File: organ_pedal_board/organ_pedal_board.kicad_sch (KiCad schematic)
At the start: 19 parts, among them J1 AudioPlug3, J2 AudioPlug3, U1 MCP6002-xSN, U3 ADS1115IDGS, U4 AP2112K-3.3

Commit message: Feat: added OLED circuit to board schematics
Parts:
- added J3: Conn_01x04, symbol Connector_Generic:Conn_01x04
- added R5, R6: 4k7, symbol Device:R
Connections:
- net GND: now also J3.1 (Pin_1)
- net dready: no longer U2.15 (D23)
- net i2c_scl: now also J3.3 (Pin_3), R6.1
- net i2c_sda: now also J3.4 (Pin_4), R5.2
- new net +3V3: J3.2 (Pin_2), R5.1, R6.2
- no-connect marks 24 -> 25
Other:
- note added: "ESP32 DevKit V1"
- note added: "OLED"
- note added: "OLED pins"
- moved on the sheet: J1, J2

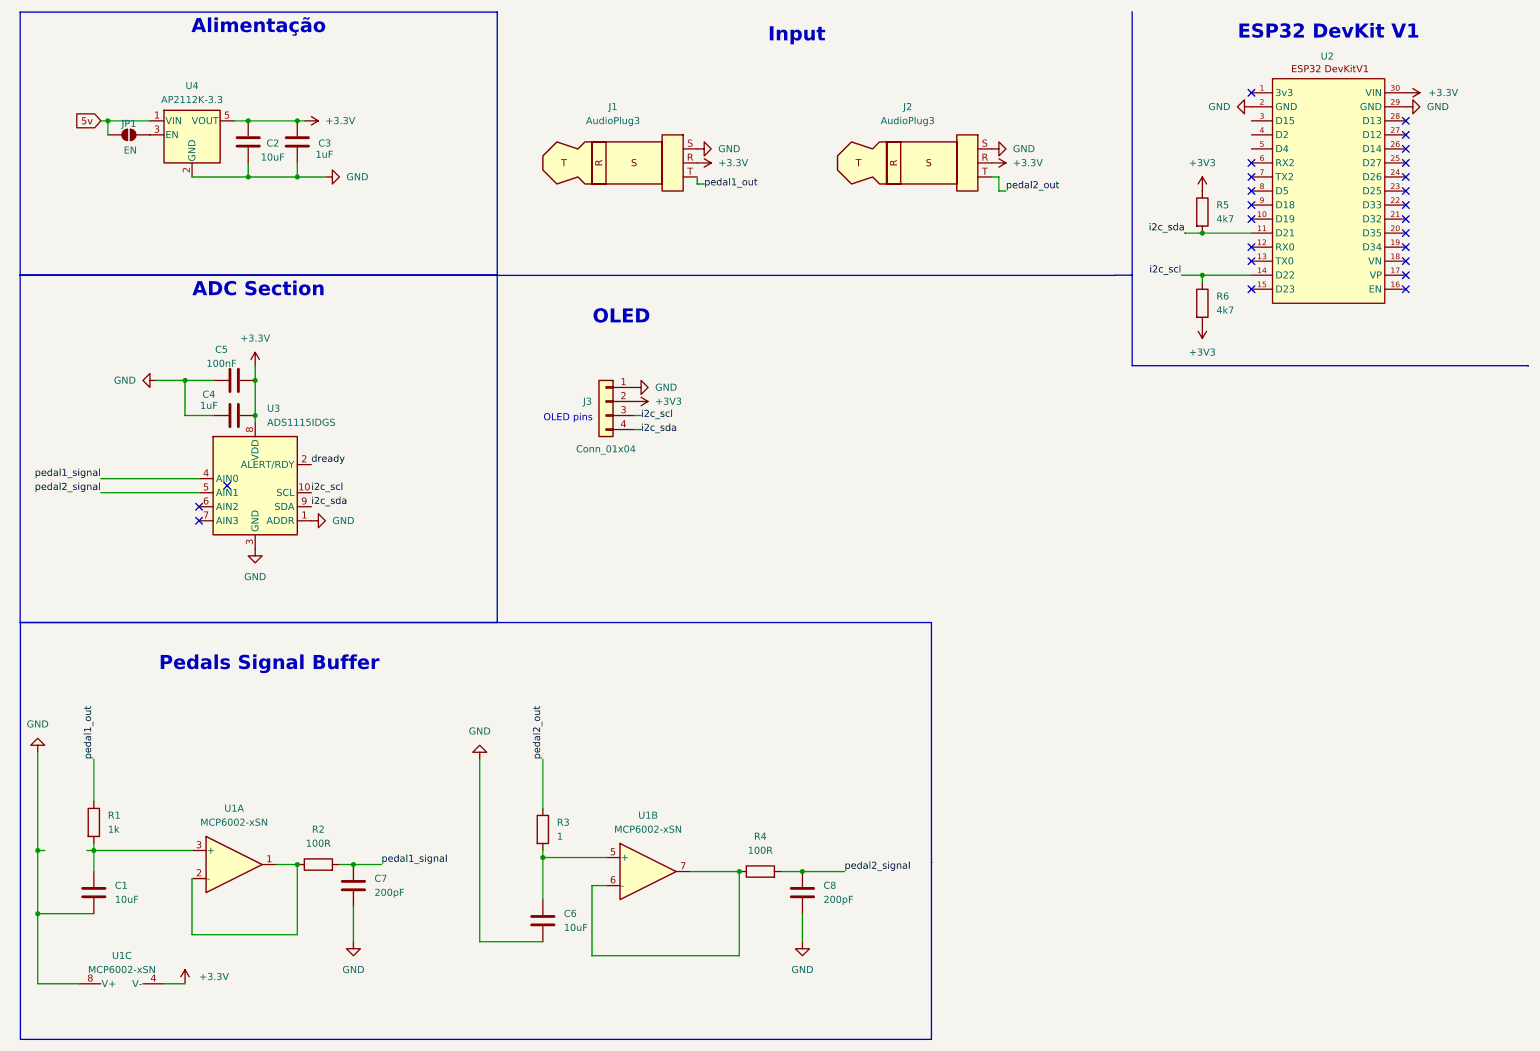
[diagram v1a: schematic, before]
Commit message: Feat: added 8 buttons and finished schematics.
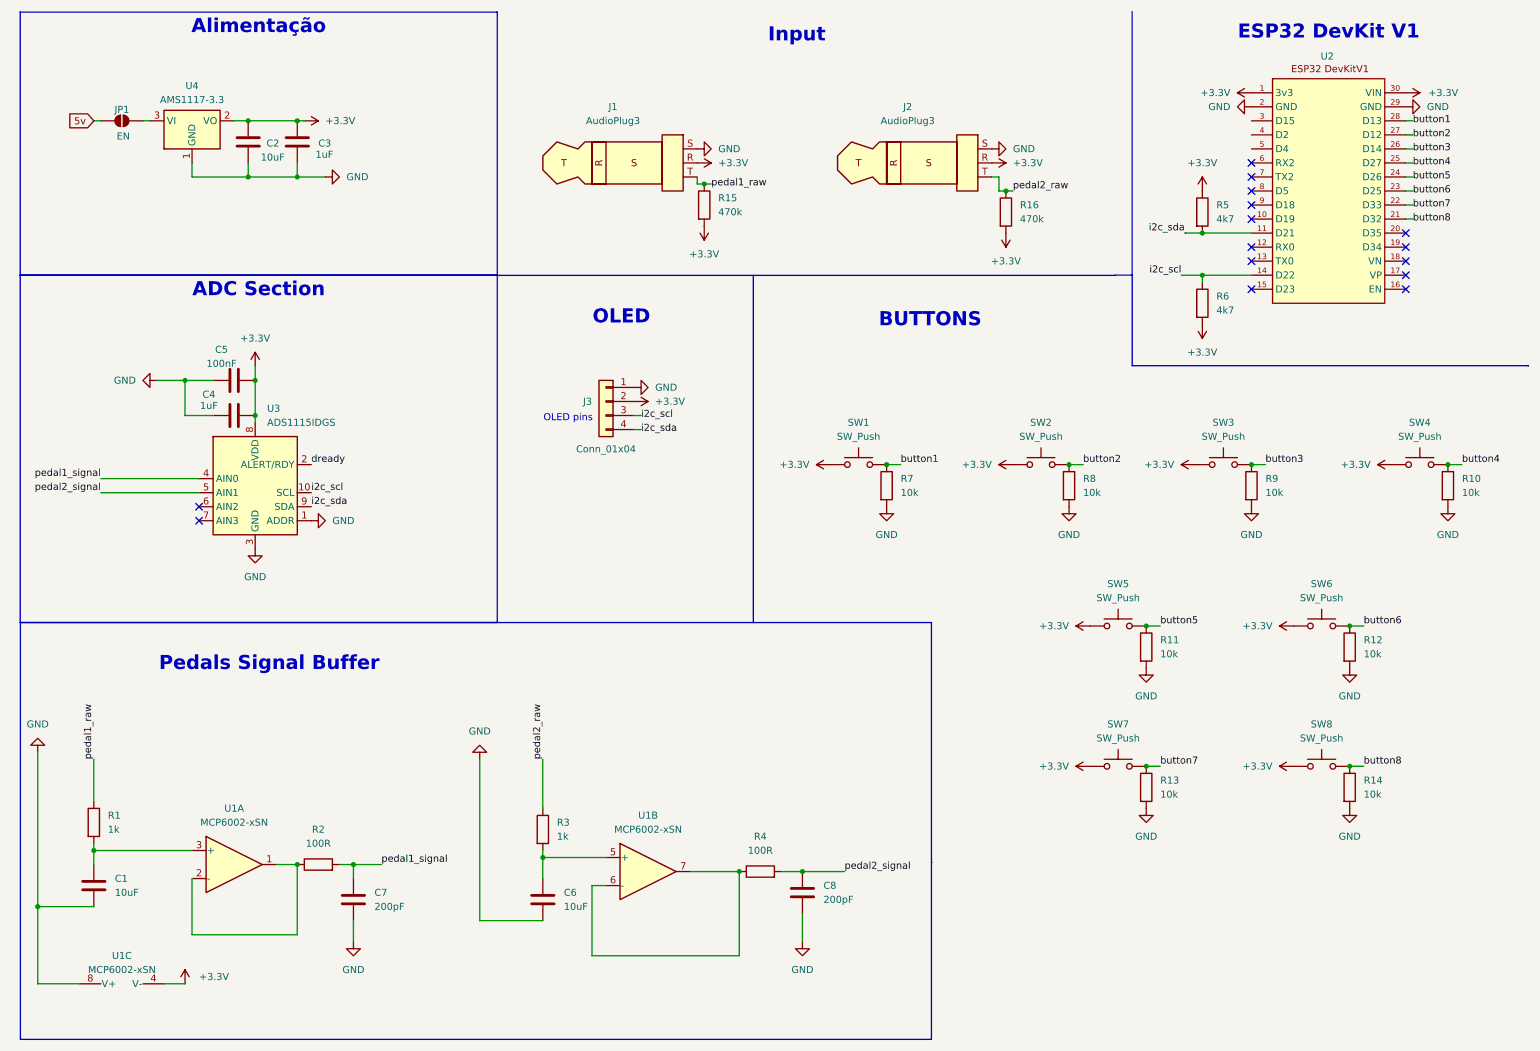
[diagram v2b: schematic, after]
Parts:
- removed U4: AP2112K-3.3, Package_TO_SOT_SMD:SOT-23-5, symbol Regulator_Linear:AP2112K-3.3
- added R10, R11, R12, R13, R14, R7, R8, R9: 10k, Resistor_THT:R_Axial_DIN0207_L6.3mm_D2.5mm_P7.62mm_Horizontal, symbol Device:R
- added R15, R16: 470k, Resistor_THT:R_Axial_DIN0207_L6.3mm_D2.5mm_P7.62mm_Horizontal, symbol Device:R
- added SW1, SW2, SW3, SW4, SW5, SW6, SW7, SW8: SW_Push, symbol Switch:SW_Push
- added U4: AMS1117-3.3, Package_TO_SOT_SMD:SOT-223-3_TabPin2, symbol Regulator_Linear:AMS1117-3.3
- C1, C2, C3, C4, C5, C6, C7, C8: footprint (none) -> Capacitor_THT:C_Disc_D10.5mm_W5.0mm_P10.00mm
- R1, R2, R4, R5, R6: footprint (none) -> Resistor_THT:R_Axial_DIN0207_L6.3mm_D2.5mm_P7.62mm_Horizontal
- R3: value 1 -> 1k; footprint (none) -> Resistor_THT:R_Axial_DIN0207_L6.3mm_D2.5mm_P7.62mm_Horizontal
- U1: footprint (none) -> Package_SO:SOIC-8_3.9x4.9mm_P1.27mm
- U3: footprint Package_SO:TSSOP-10_3x3mm_P0.5mm -> (none)
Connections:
- net +3V3 is gone; now on net +3.3V: J3.2 (Pin_2), R5.1, R6.2
- net +3.3V: now also U2.1 (3v3), R15.2, R16.2, SW1.1, SW2.1, SW3.1, SW4.1, SW5.1, SW6.1, SW7.1, SW8.1, U4.2 (VO)
- net GND: now also R10.2, R11.2, R12.2, R13.2, R14.2, R7.2, R8.2, R9.2, U4.1 (GND)
- net at JP1.2 (B): now also U4.3 (VI)
- net button8: now reaches U2.21 (D32)
- net button8: now also R14.1, SW8.2
- net button7: now reaches U2.22 (D33)
- net button7: now also R13.1, SW7.2
- net button6: now reaches U2.23 (D25)
- net button6: now also R12.1, SW6.2
- net button5: now reaches U2.24 (D26)
- net button5: now also R11.1, SW5.2
- net button4: now reaches U2.25 (D27)
- net button4: now also R10.1, SW4.2
- net button3: now reaches U2.26 (D14)
- net button3: now also R9.1, SW3.2
- net button2: now reaches U2.27 (D12)
- net button2: now also R8.1, SW2.2
- net button1: now reaches U2.28 (D13)
- net button1: now also R7.1, SW1.2
- net pedal1_out renamed pedal1_raw
- net pedal1_raw: now also R15.1
- net pedal2_out renamed pedal2_raw
- net pedal2_raw: now also R16.1
- no-connect marks 25 -> 15
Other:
- note added: "BUTTONS"
- title: (none) -> ESP32_MIDI_Controller
- moved on the sheet: C1, C6, C7, JP1

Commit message: Refactor code structure for improved readability and maintainability
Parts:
- removed C2: 10uF, Capacitor_THT:C_Disc_D10.5mm_W5.0mm_P10.00mm, symbol Device:C
- removed C3: 1uF, Capacitor_THT:C_Disc_D10.5mm_W5.0mm_P10.00mm, symbol Device:C
- removed J1, J2: AudioPlug3, symbol Connector_Audio:AudioPlug3
- removed JP1: EN, symbol Jumper:SolderJumper_2_Open
- removed U3: ADS1115IDGS, symbol Analog_ADC:ADS1115IDGS
- removed U4: AMS1117-3.3, Package_TO_SOT_SMD:SOT-223-3_TabPin2, symbol Regulator_Linear:AMS1117-3.3
- added J2, J3: NMJ6HFD2, Connector_Audio:Jack_6.35mm_Neutrik_NMJ6HFD2_Horizontal, symbol Connector_Audio:NMJ6HFD2
- added J4: ADS1115_conn, Connector_PinSocket_2.54mm:PinSocket_1x10_P2.54mm_Vertical, symbol Connector_Generic:Conn_01x10
- added R17: 10k, Resistor_THT:R_Axial_DIN0207_L6.3mm_D2.5mm_P5.08mm_Vertical, symbol Device:R
- added SW9: SW_Push, Button_Switch_THT:SW_PUSH_6mm, symbol Switch:SW_Push
- J1: renamed from J3; footprint (none) -> Connector_PinSocket_2.54mm:PinSocket_1x04_P2.54mm_Vertical
- R1, R10, R11, R12, R13, R14, R2, R3, R4, R5, R6, R7, R8, R9: footprint Resistor_THT:R_Axial_DIN0207_L6.3mm_D2.5mm_P7.62mm_Horizontal -> Resistor_THT:R_Axial_DIN0207_L6.3mm_D2.5mm_P5.08mm_Vertical
- R15, R16: value 470k -> 10k; footprint Resistor_THT:R_Axial_DIN0207_L6.3mm_D2.5mm_P7.62mm_Horizontal -> Resistor_THT:R_Axial_DIN0207_L6.3mm_D2.5mm_P5.08mm_Vertical
- SW1, SW2, SW3, SW4, SW5, SW6, SW7, SW8: footprint (none) -> Connector_JST:JST_XH_S2B-XH-A-1_1x02_P2.50mm_Horizontal
- U2: footprint (none) -> MyDesigns:esp32_devkit_v1_doit
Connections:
- net +3.3V: now also J2.R, J3.R, J4.1 (Pin_1), SW9.1; no longer U2.30 (VIN)
- net GND: now also J2.S, J3.S, J4.2 (Pin_2), J4.5 (Pin_5), R17.2
- net dready: now also J4.6 (Pin_6)
- net i2c_scl: now also J4.3 (Pin_3)
- net i2c_sda: now also J4.4 (Pin_4)
- net pedal1_raw: now also J2.T; no longer R15.1
- net pedal1_signal: now also J4.7 (Pin_7)
- net pedal2_raw: now also J3.T; no longer R16.1
- net pedal2_signal: now also J4.8 (Pin_8)
- net config_button: now reaches U2.3 (D15)
- net config_button: now also R17.1, SW9.2
- new net: J3.TN, R16.1
- new net: J2.TN, R15.1
- no-connect marks 15 -> 22
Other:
- moved on the sheet: C4, C5, J1, R15, R16, R5, R6

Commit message: Fix: Corrected MCP6002 power supply, corrected P10 plug 1 MCP6002  signal output
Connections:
- net +3.3V: now also C1.2, U1.8 (V+); no longer U1.4 (V-)
- net GND: now also U1.4 (V-); no longer C1.2, U1.8 (V+)
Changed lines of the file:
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@@
 	)
 	(junction
-		(at 19.05 173.99)
-		(diameter 0)
-		(color 0 0 0 0)
-	)
-	(junction
 		(at 252.73 148.59)
 		(diameter 0)
@@
 	)
 	(junction
+		(at 19.05 173.99)
+		(diameter 0)
+		(color 0 0 0 0)
+	)
+	(junction
 		(at 57.15 76.2)
 		(diameter 0)
@@
 	(wire
 		(pts
-			(xy 19.05 146.05) (xy 19.05 173.99)
-		)
-		(stroke
-			(width 0)
-			(type default)
-		)
-	)
-	(wire
-		(pts
 			(xy 57.15 76.2) (xy 60.96 76.2)
 		)
@@
 	(wire
 		(pts
+			(xy 19.05 142.24) (xy 19.05 173.99)
+		)
+		(stroke
+			(width 0)
+			(type default)
+		)
+	)
+	(wire
+		(pts
 			(xy 264.16 36.83) (xy 262.89 36.83)
 		)
@@
 		)
 	)
-	(wire
-		(pts
-			(xy 38.1 187.96) (xy 41.91 187.96)
-		)
-		(stroke
-			(width 0)
-			(type default)
-		)
-	)
 	(polyline
 		(pts
@@
 	(wire
 		(pts
+			(xy 40.64 187.96) (xy 38.1 187.96)
+		)
+		(stroke
+			(width 0)
+			(type default)
+		)
+	)
+	(wire
+		(pts
 			(xy 53.34 83.82) (xy 60.96 83.82)
 		)
@@
 	(symbol
 		(lib_id "power:+5V")
-		(at 41.91 187.96 0)
+		(at 19.05 142.24 0)
 		(unit 1)
 		(exclude_from_sim no)
@@
 		(on_board yes)
 		(dnp no)
-		(fields_autoplaced yes)
 		(property "Reference" "#PWR03"
-			(at 41.91 191.77 0)
+			(at 19.05 146.05 0)
 			(effects
 				(font
@@
 		)
 		(property "Value" "+3.3V"
-			(at 44.45 186.6899 0)
+			(at 19.05 138.176 0)
 			(effects
 				(font
 					(size 1.27 1.27)
 				)
-				(justify left)
+				(justify bottom)
 			)
 		)
 		(property "Footprint" ""
-			(at 41.91 187.96 0)
+			(at 19.05 142.24 0)
 			(effects
 				(font
@@
 		)
 		(property "Datasheet" ""
-			(at 41.91 187.96 0)
+			(at 19.05 142.24 0)
 			(effects
 				(font
@@
 		)
 		(property "Description" ""
-			(at 41.91 187.96 0)
+			(at 19.05 142.24 0)
 			(effects
 				(font
@@
 	(symbol
 		(lib_id "power:GND")
-		(at 19.05 146.05 180)
+		(at 40.64 187.96 90)
 		(unit 1)
 		(exclude_from_sim no)
@@
 		(fields_autoplaced yes)
 		(property "Reference" "#PWR01"
-			(at 19.05 139.7 0)
+			(at 46.99 187.96 0)
 			(effects
 				(font
@@
 		)
 		(property "Value" "GND"
-			(at 19.05 140.97 0)
+			(at 44.45 187.9599 90)
 			(effects
 				(font
 					(size 1.27 1.27)
 				)
+				(justify right)
 			)
 		)
 		(property "Footprint" ""
-			(at 19.05 146.05 0)
+			(at 40.64 187.96 0)
 			(effects
 				(font
@@
 		)
 		(property "Datasheet" ""
-			(at 19.05 146.05 0)
+			(at 40.64 187.96 0)
 			(effects
 				(font
@@
 		)
 		(property "Description" ""
-			(at 19.05 146.05 0)
+			(at 40.64 187.96 0)
 			(effects
 				(font

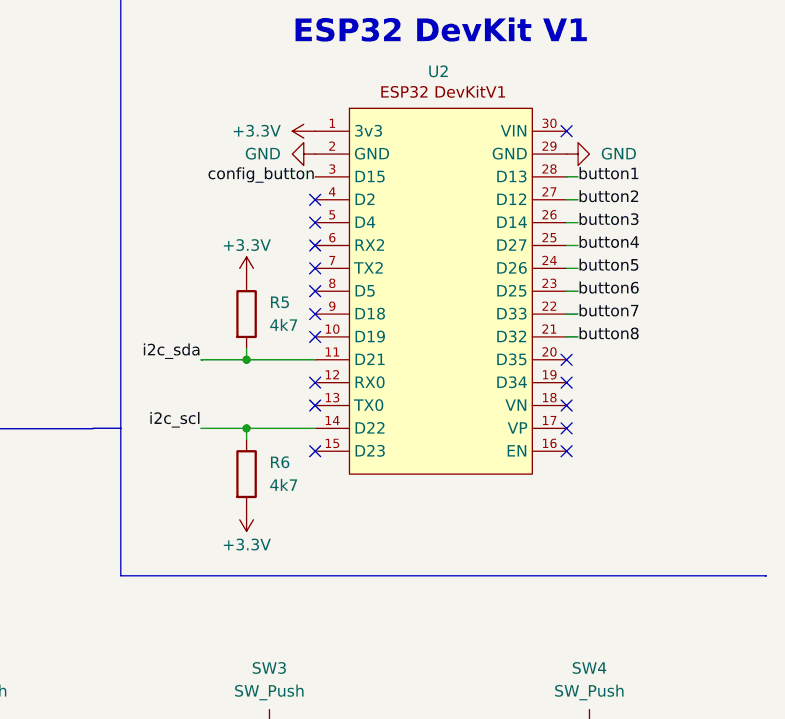
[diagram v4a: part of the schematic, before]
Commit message: Fix: Corrected vias and esp32 pin assignment
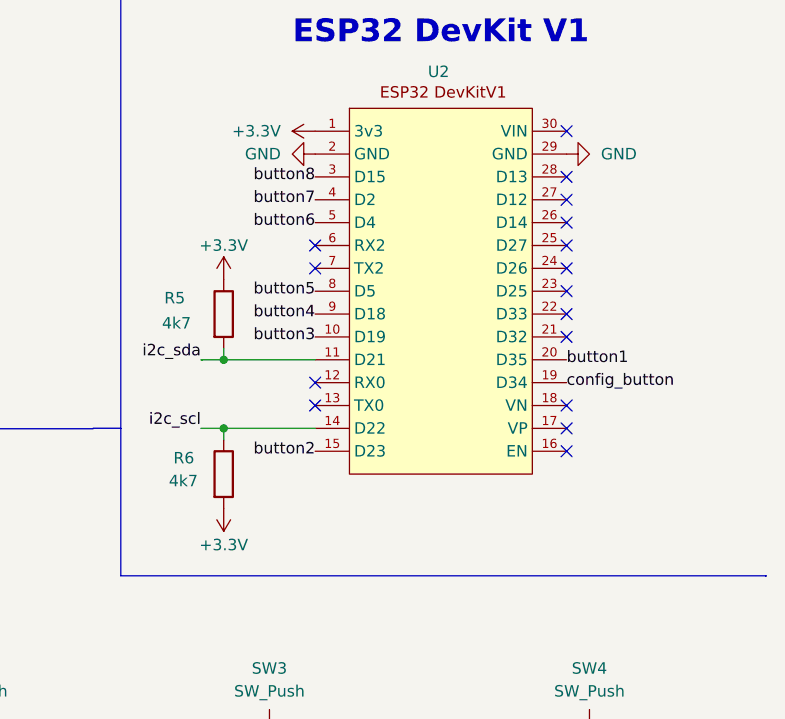
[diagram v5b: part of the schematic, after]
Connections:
- net button1: now also U2.20 (D35); no longer U2.28 (D13)
- net button2: now also U2.15 (D23); no longer U2.27 (D12)
- net button3: now also U2.10 (D19); no longer U2.26 (D14)
- net button4: now also U2.9 (D18); no longer U2.25 (D27)
- net button5: now also U2.8 (D5); no longer U2.24 (D26)
- net button6: now also U2.5 (D4); no longer U2.23 (D25)
- net button7: now also U2.4 (D2); no longer U2.22 (D33)
- net button8: now also U2.3 (D15); no longer U2.21 (D32)
- net config_button: now also U2.19 (D34); no longer U2.3 (D15)
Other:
- moved on the sheet: R5, R6
